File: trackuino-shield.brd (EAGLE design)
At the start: 67.3 x 53.3 mm, 26 parts, among them IC2 REG1117, IC3 ON M74VHC1GT125DT1G, IC4 ON M74VHC1GT125DT1G, IC5 ON M74VHC1GT125DT1G, J5 J5MM, J6 J5MM, J7 J5MM, J8 J5MM, M2 HX1, M3 VENUS634FLPX, Q1 PMV20XN, PMV16UN, etc, U1 LM60 int, X1 BU-SMA-V, X2 Vin, X3 LM60 ext, X4 Buzzer

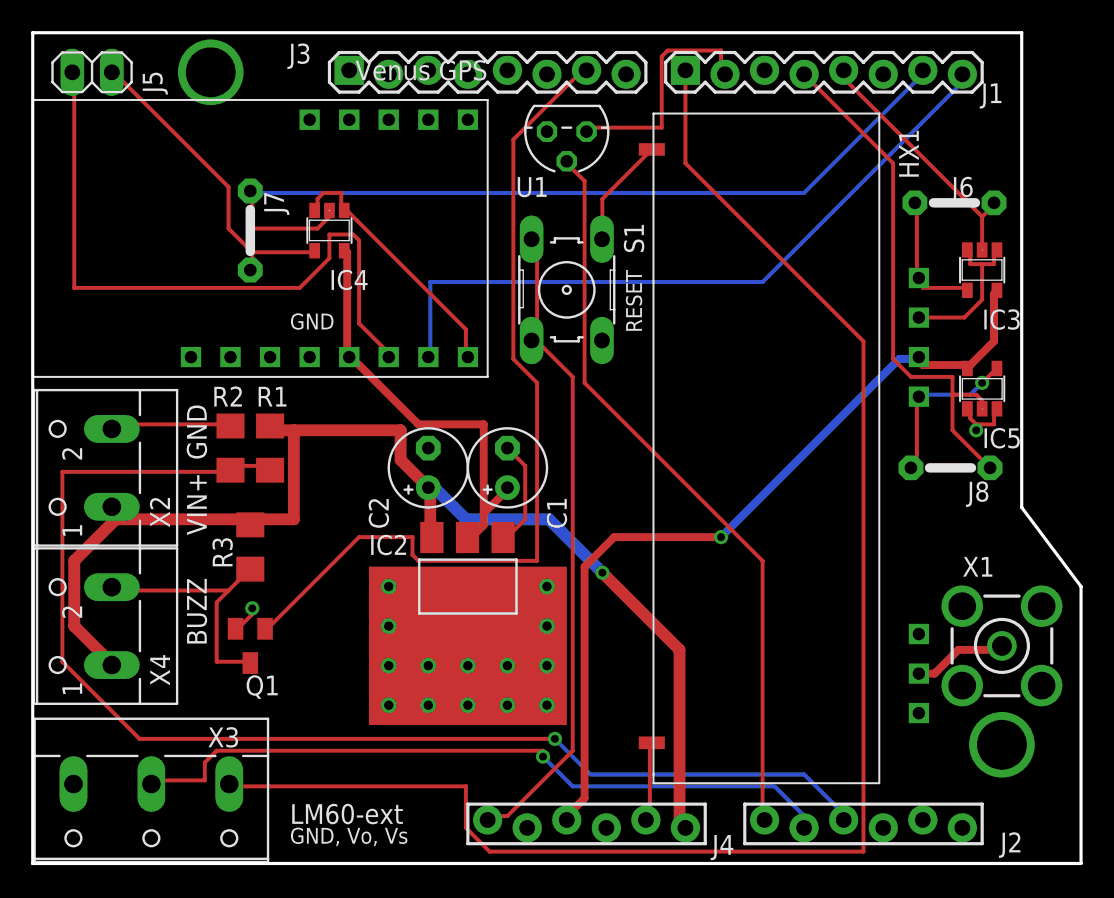
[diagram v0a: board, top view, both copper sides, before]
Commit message: Replaced Venus 634FLPx (phased out) with 638FLPx (sparkfun product #11058)
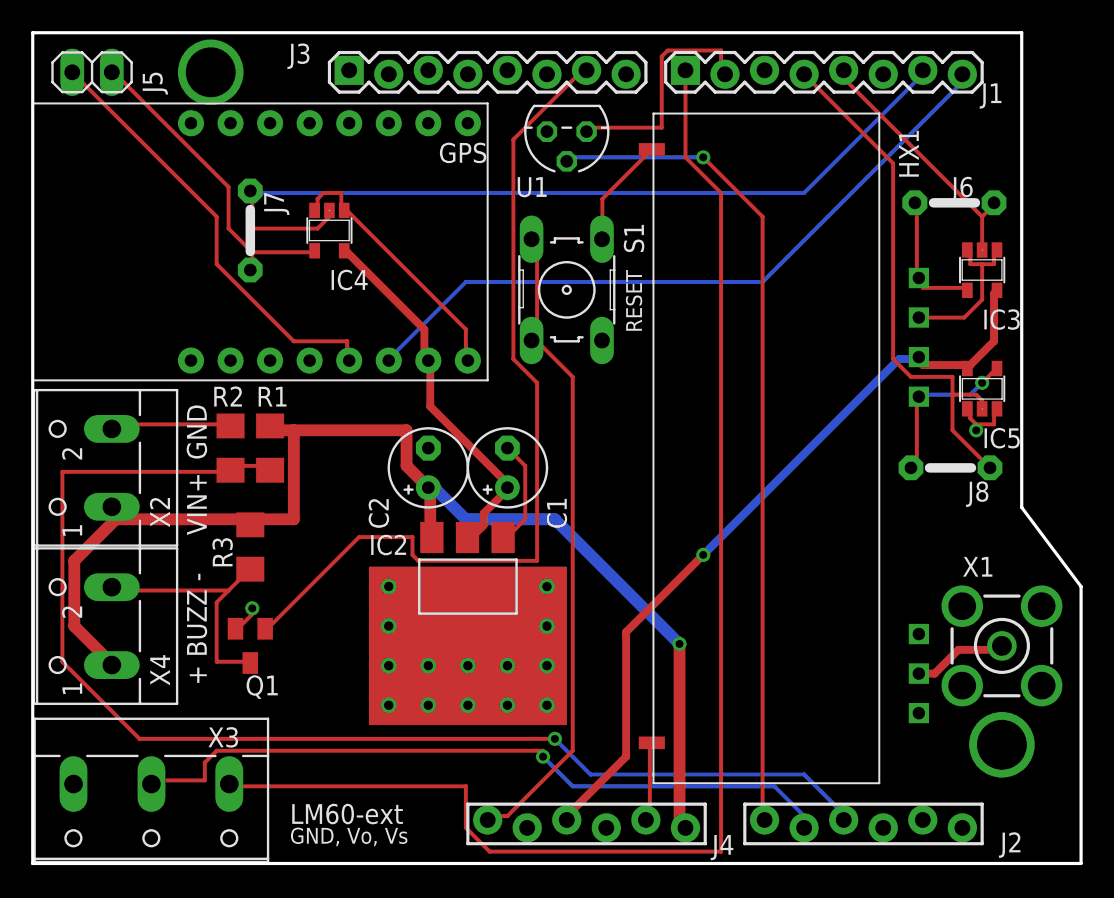
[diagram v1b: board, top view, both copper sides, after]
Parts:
- removed M3: VENUS634FLPX, trackuino:VENUS634FLPX
- added GPS: VENUS638FLPX, trackuino:VENUS638FLPX
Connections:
- net +3V3: now also GPS.3.3V; no longer M3.3.3V
- net GND: now also GPS.GND; no longer M3.GND
- net N$2: now also GPS.RX0; no longer M3.RX
- net RX: now also GPS.TX0; no longer M3.TX
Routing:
- net N$2: track 42.9 -> 27.9 mm
- net D7: track 98.9 -> 86.0 mm
- net A0: track 47.5 -> 53.2 mm, vias 0 -> 1
- net +5V: track 53.2 -> 49.2 mm
- net +3V3: track 27.5 -> 24.0 mm
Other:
- board text added: "+ BUZZ -"
- board text removed: "BUZZ"

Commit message: Updated footprint of the GPS to the newest breakout board for the (Venus638FLPx)
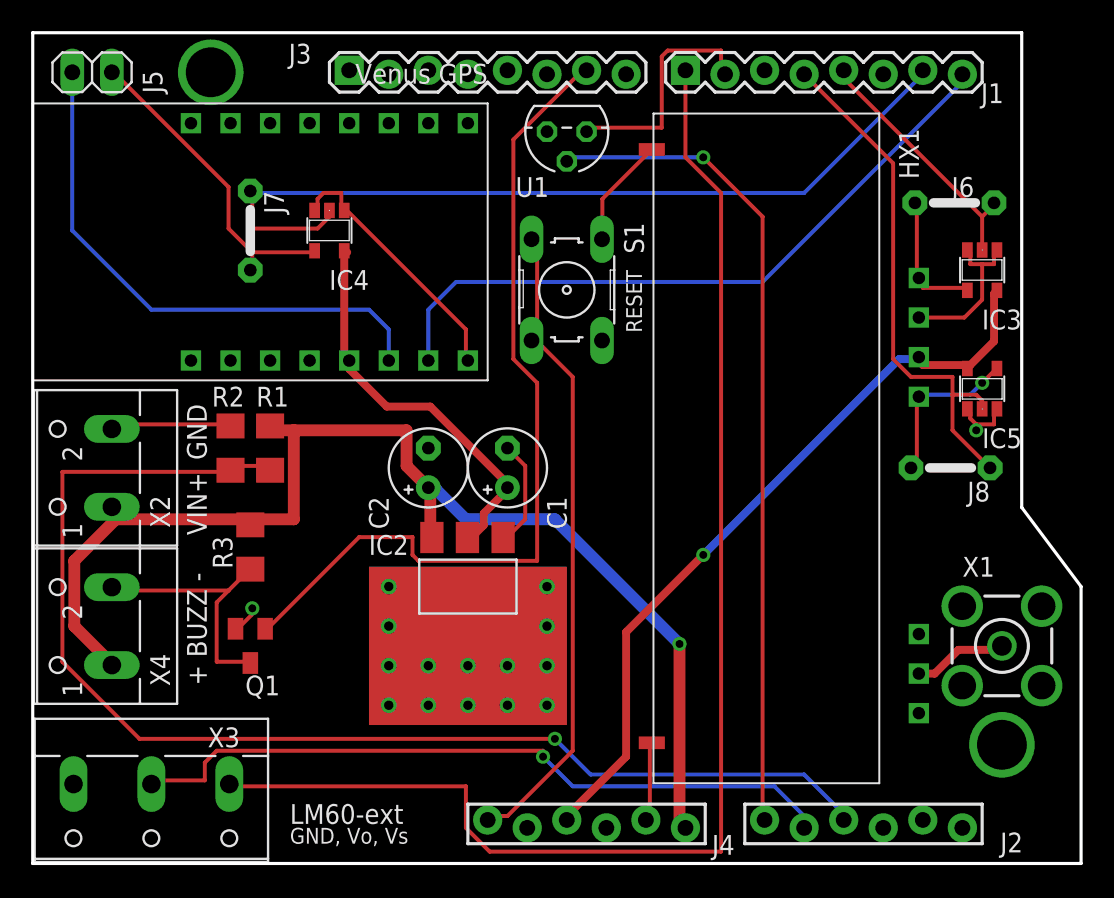
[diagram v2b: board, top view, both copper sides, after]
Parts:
- removed GPS: VENUS638FLPX, trackuino:VENUS638FLPX
- added M1: VENUS638FLPX, Venus638FLPx:VENUS638FLPX
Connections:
- net +3V3: now also M1.3V3; no longer GPS.3.3V
- net GND: now also M1.GND; no longer GPS.GND
- net N$2: now also M1.RX0; no longer GPS.RX0
- net RX: now also M1.TX0; no longer GPS.TX0
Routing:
- net N$2: track 27.9 -> 35.1 mm
- net +3V3: track 24.0 -> 25.8 mm
- net RX: track 44.9 -> 44.3 mm
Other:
- board text added: "Trackuino Shield 2.3"
- board text removed: "Trackuino Shield 2.2"
